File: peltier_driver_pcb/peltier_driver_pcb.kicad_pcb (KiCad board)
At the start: 2 copper layers, 10 parts, among them J1 Conn_01x04, U1 OLED_128x32_I2C, U2 INA260

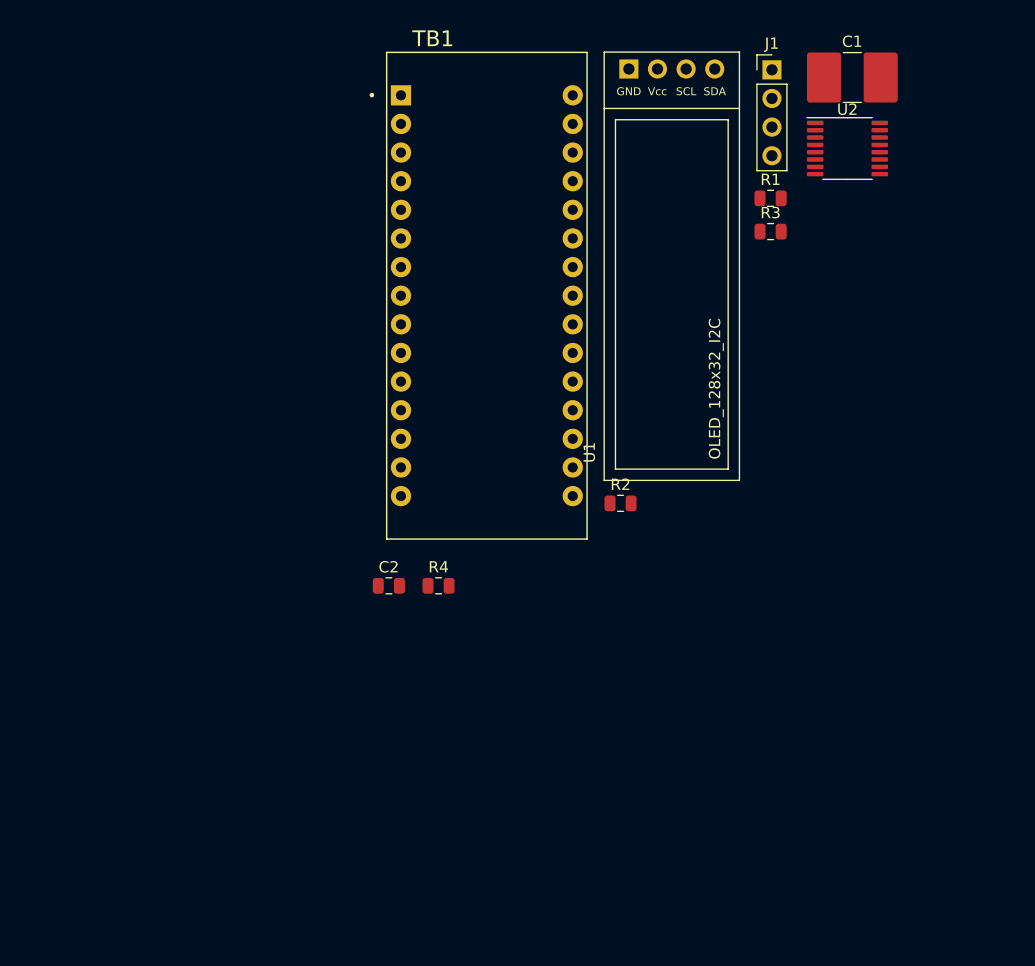
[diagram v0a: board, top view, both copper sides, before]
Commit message: properly saved 3D models to footprint files
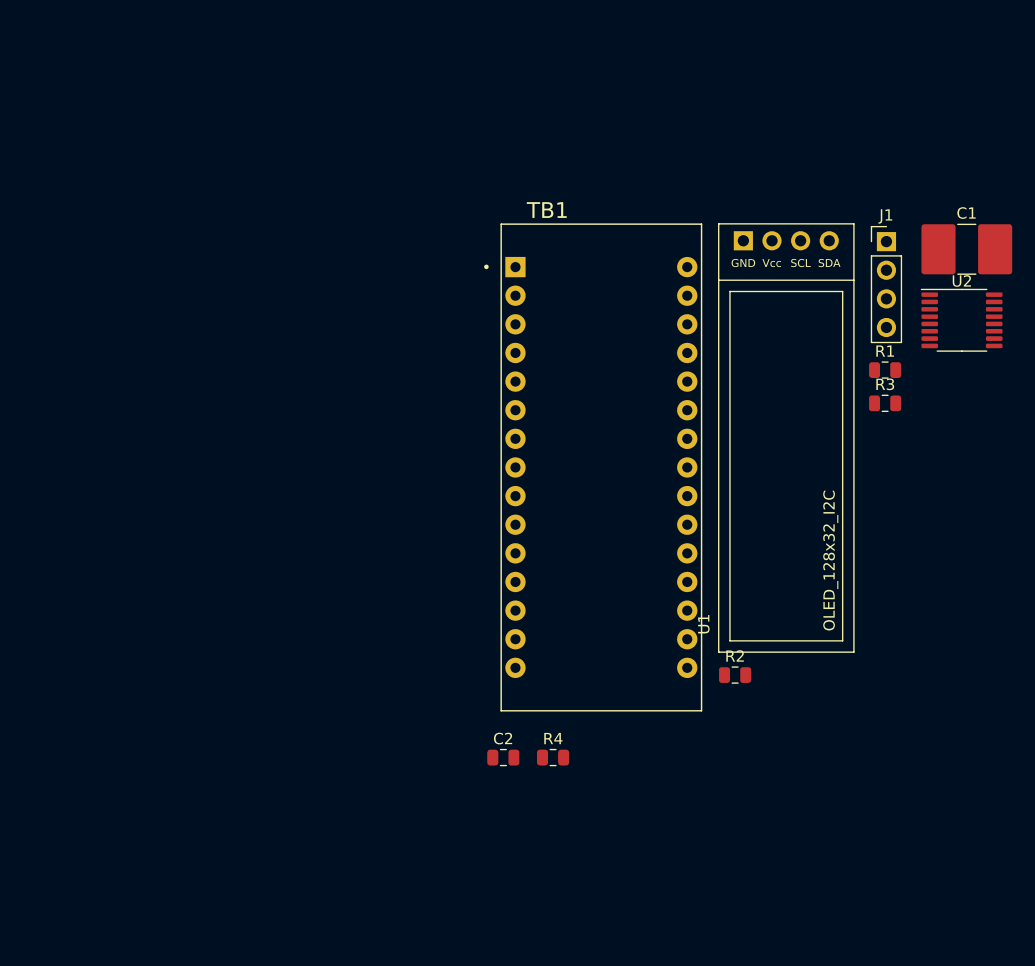
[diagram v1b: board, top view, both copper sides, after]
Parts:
- moved R2 18.3 mm to (167.0, 87.3)
- moved C2 18.3 mm to (146.5, 94.6)
- moved C1 18.3 mm to (187.6, 49.5)
- moved J1 18.3 mm to (180.5, 48.8)
- moved R1 18.3 mm to (180.4, 60.2)
- moved TB1 18.3 mm to (155.2, 68.9)
- moved U1 18.3 mm to (165.6, 47.2)
- moved U2 18.3 mm to (187.2, 55.8)
- moved R3 18.3 mm to (180.4, 63.2)
- moved R4 18.3 mm to (150.9, 94.6)

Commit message: updating PCB
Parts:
- added J2: Temp_sensor_A, Connector_PinHeader_2.54mm:PinHeader_1x02_P2.54mm_Vertical, F.Cu at (113.0, 101.3)
- added J3: Temp_sensor_B, Connector_PinHeader_2.54mm:PinHeader_1x02_P2.54mm_Vertical, F.Cu at (120.1, 101.3)
- added R5: 10k, Resistor_SMD:R_0805_2012Metric, F.Cu at (119.6, 78.7)
- added R6: 10k, Resistor_SMD:R_0805_2012Metric, F.Cu at (121.9, 78.6)
- added R7: 10k, Resistor_SMD:R_0805_2012Metric, F.Cu at (119.6, 82.4)
- added R8: 10k, Resistor_SMD:R_0805_2012Metric, F.Cu at (121.9, 82.4)
- added RV1: 10k, Potentiometer_THT:Potentiometer_Bourns_3296W_Vertical, F.Cu at (114.6, 97.0)
- added RV2: 10k, Potentiometer_THT:Potentiometer_Bourns_3296W_Vertical, F.Cu at (121.5, 97.0)
- moved U2 81.1 mm to (106.6, 65.5), turned to 90 degrees
- moved C1 77.7 mm to (110.0, 53.1)
- moved R3 70.1 mm to (110.4, 67.5), turned to 270 degrees
- moved R1 58.7 mm to (121.9, 54.6), turned to 270 degrees
- moved R2 58.3 mm to (119.4, 53.7), turned to 270 degrees
- moved U1 54.3 mm to (112.0, 56.1)
- moved C2 51.6 mm to (108.3, 59.9), turned to 90 degrees
- moved R4 51.0 mm to (110.4, 63.6), turned to 90 degrees
- moved J1 46.6 mm to (146.1, 80.3), turned to 180 degrees
- moved TB1 23.3 mm to (133.6, 77.7), turned to 180 degrees
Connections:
- C2 pad 1: Net-(C2-Pad1) -> +5V
- R3 pad 1: +5V -> +3V3
- R4 pad 1: +5V -> +3V3
- TB1 pad 23: Net-(TB1-Pad23) -> T_A0
- TB1 pad 24: Net-(TB1-Pad24) -> T_B0
- TB1 pad 25: Net-(TB1-Pad25) -> T_A1
- TB1 pad 26: Net-(TB1-Pad26) -> T_B1
- U2 pad 10: Net-(C2-Pad1) -> +5V
- U2 pad 4: Net-(U2-Pad4) -> GND
- U2 pad 5: Net-(U2-Pad5) -> GND
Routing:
- net SDA: track 0.00 -> 60.1 mm
- net SCL: track 0.00 -> 58.6 mm
- net T_A1: track 0.00 -> 25.7 mm
- net T_B1: track 0.00 -> 19.2 mm
- net T_B0: track 0.00 -> 7.61 mm
- net +3V3: track 0.00 -> 6.50 mm
- net T_A0: track 0.00 -> 6.42 mm
- net +5V: track 0.00 -> 1.86 mm

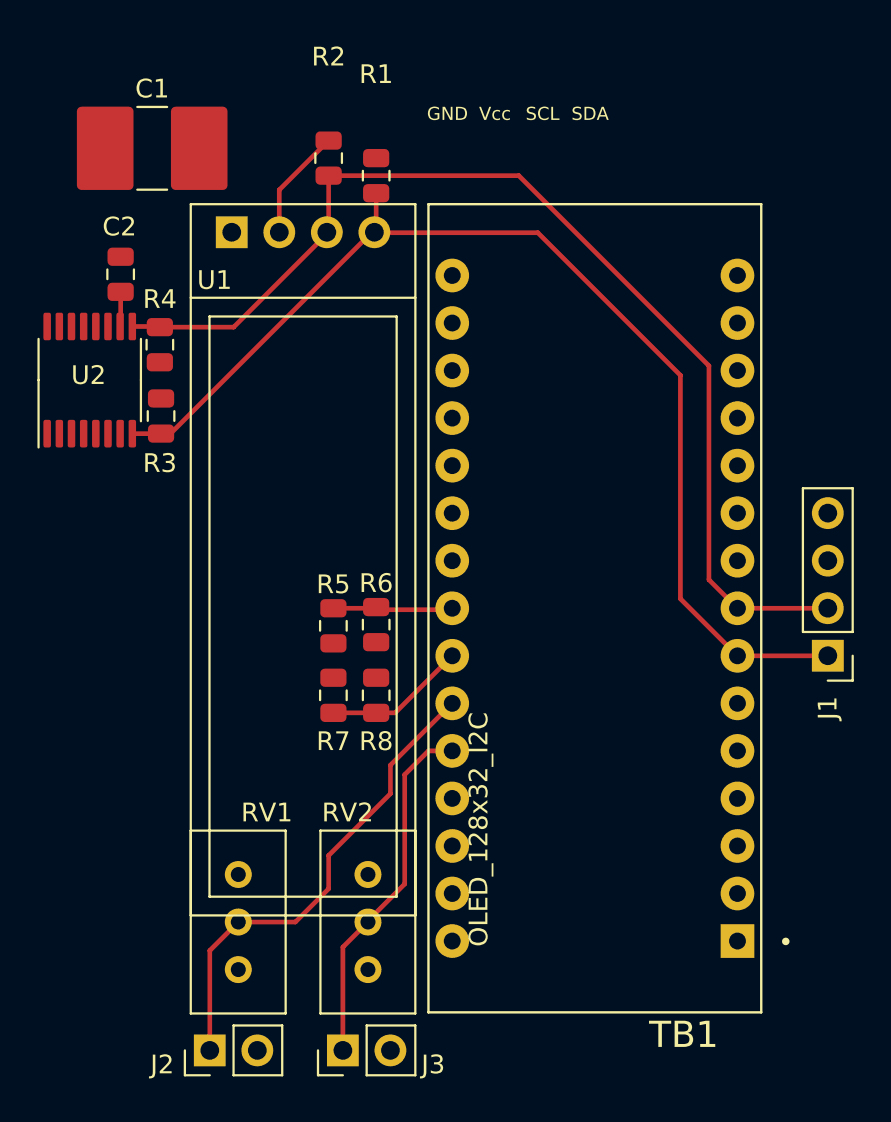
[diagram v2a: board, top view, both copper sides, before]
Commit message: single Pt1000, wheatstone bridge diff amplifier
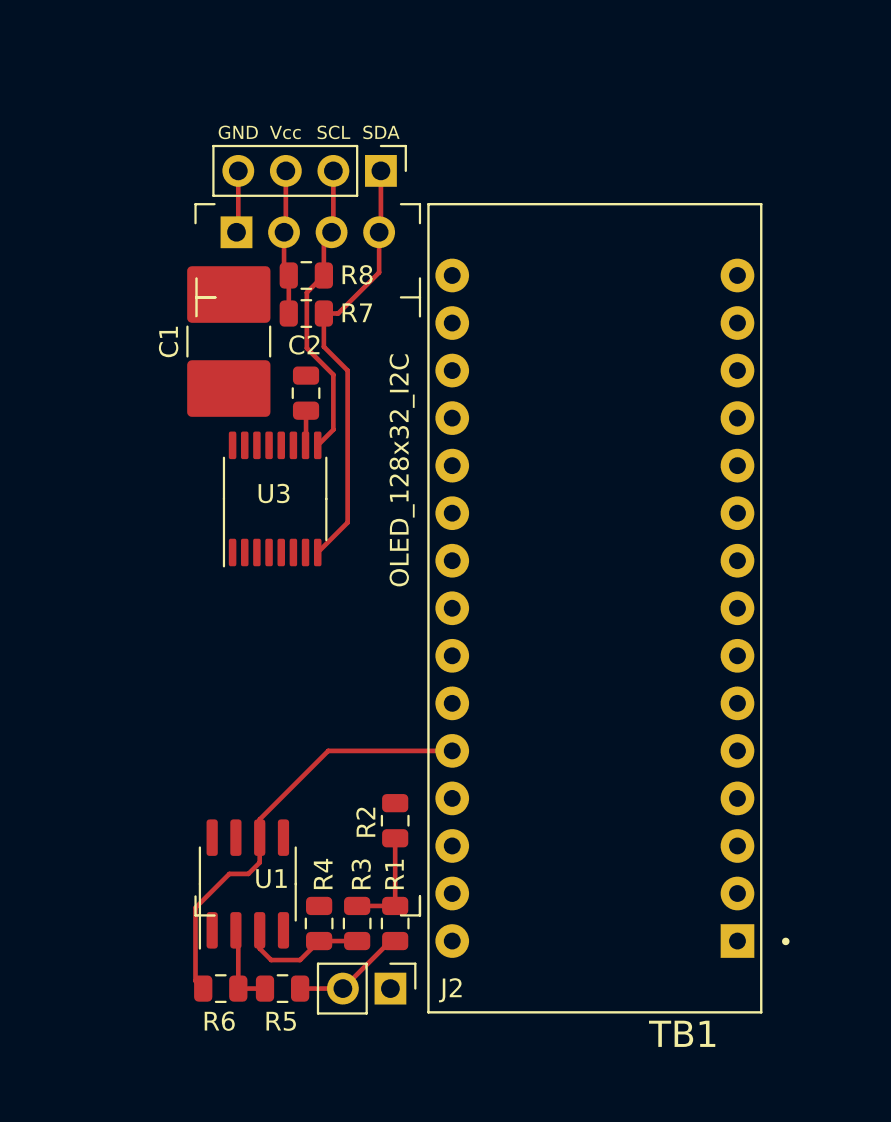
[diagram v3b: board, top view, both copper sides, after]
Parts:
- removed J3: Temp_sensor_B, Connector_PinHeader_2.54mm:PinHeader_1x02_P2.54mm_Vertical
- removed the R7 at (119.6, 82.4)
- removed RV1, RV2: 10k, Potentiometer_THT:Potentiometer_Bourns_3296W_Vertical
- added R3: 1K, Resistor_SMD:R_0805_2012Metric, F.Cu at (120.9, 94.6)
- added U2: OLED_128x32_I2C, peltier_driver_pcb:OLED_128x32_I2C, F.Cu at (112.3, 56.1)
- J2: value Temp_sensor_A -> Pt1000_top
- R1: value 4k7 -> 1K
- R2: value 4k7 -> 4K
- R4: value 4K7 -> 1K
- R5, R6: value 10k -> 100k
- R8: value 10k -> 4K7
- U1: value OLED_128x32_I2C -> MCP601-xSN; footprint peltier_driver_pcb:OLED_128x32_I2C -> Package_SO:SOIC-8_3.9x4.9mm_P1.27mm
- moved R1 40.0 mm to (122.9, 94.6)
- moved U1 36.4 mm to (115.1, 92.5), turned to 90 degrees
- moved R2 35.6 mm to (122.9, 89.1)
- moved J1 35.2 mm to (122.2, 54.4), turned to 270 degrees
- moved R4 32.1 mm to (118.9, 94.6)
- moved R8 22.7 mm to (118.2, 59.9), turned to 0 degrees
- moved R6 21.1 mm to (113.6, 98.0), turned to 0 degrees
- moved R5 19.6 mm to (116.9, 98.0), turned to 0 degrees
- moved C2 11.8 mm to (118.2, 66.2)
- moved U3 11.8 mm to (116.5, 71.9)
- moved C1 11.1 mm to (114.0, 63.5), turned to 90 degrees
- moved J2 10.2 mm to (122.7, 98.0), turned to 270 degrees
- moved R7 9.50 mm to (118.2, 62.0), turned to 0 degrees
- renumbered R3 to R7, U2 to U3
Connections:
- J2 pad 1: T_A1 -> GND
- J2 pad 2: GND -> Net-(J2-Pad2)
- R1 pad 1: +3V3 -> Net-(R1-Pad1)
- R1 pad 2: SDA -> Net-(J2-Pad2)
- R2 pad 1: +3V3 -> +5V
- R2 pad 2: SCL -> Net-(R1-Pad1)
- R4 pad 1: +3V3 -> Net-(R3-Pad2)
- R4 pad 2: SCL -> GND
- R5 pad 1: +5V -> Net-(R5-Pad1)
- R5 pad 2: T_A0 -> Net-(J2-Pad2)
- R6 pad 1: T_A0 -> T_sense
- R6 pad 2: GND -> Net-(R5-Pad1)
- R8 pad 1: T_B0 -> +3V3
- R8 pad 2: GND -> SCL
- TB1 pad 23: T_A0 -> Net-(TB1-Pad23)
- TB1 pad 24: T_B0 -> Net-(TB1-Pad24)
- TB1 pad 25: T_A1 -> Net-(TB1-Pad25)
- TB1 pad 26: T_B1 -> T_sense
- U1 pad 1: +3V3 -> Net-(U1-Pad1)
- U1 pad 2: SCL -> Net-(R5-Pad1)
- U1 pad 3: SDA -> Net-(R3-Pad2)
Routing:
- net SCL: track 58.6 -> 16.2 mm
- net SDA: track 60.1 -> 23.3 mm
- net T_A1: track 25.7 -> 0.00 mm
- net T_sense: track 0.00 -> 23.0 mm
- net T_B1: track 19.2 -> 0.00 mm
- net T_B0: track 7.61 -> 0.00 mm
- net Net-(R3-Pad2): track 0.00 -> 6.86 mm
- net T_A0: track 6.42 -> 0.00 mm
- net Net-(J2-Pad2): track 0.00 -> 6.13 mm
- net Net-(R1-Pad1): track 0.00 -> 5.65 mm
- net Net-(R5-Pad1): track 0.00 -> 4.59 mm
- net GND: track 0.00 -> 3.32 mm
- net +3V3: track 6.50 -> 8.27 mm

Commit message: some tweaks
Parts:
- added V+: Peltier_A, Connector_Pin:Pin_D1.0mm_L10.0mm, F.Cu at (113.0, 77.7)
- added V-: Peltier_B, Connector_Pin:Pin_D1.0mm_L10.0mm, F.Cu at (113.0, 67.1)
- C1: footprint Capacitor_SMD:C_2816_7142Metric -> Capacitor_SMD:C_0805_2012Metric
- moved C1 3.97 mm to (116.1, 66.9)
- moved U3 1.08 mm to (115.6, 72.4)
- moved C2 0.51 mm to (118.1, 66.7)
- moved U1 0.25 mm to (114.8, 92.5)
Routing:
- net SCL: track 16.2 -> 55.0 mm
- net SDA: track 23.3 -> 45.1 mm
- net IN-: track 0.00 -> 2.87 mm
- net IN+: track 0.00 -> 2.87 mm
- net +5V: track 1.86 -> 3.15 mm
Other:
- board outline added: 32.3 x 48.8 mm
- net class Vcc added: clearance 0.2, trace_width 0.5, via_dia 0.8, via_drill 0.4

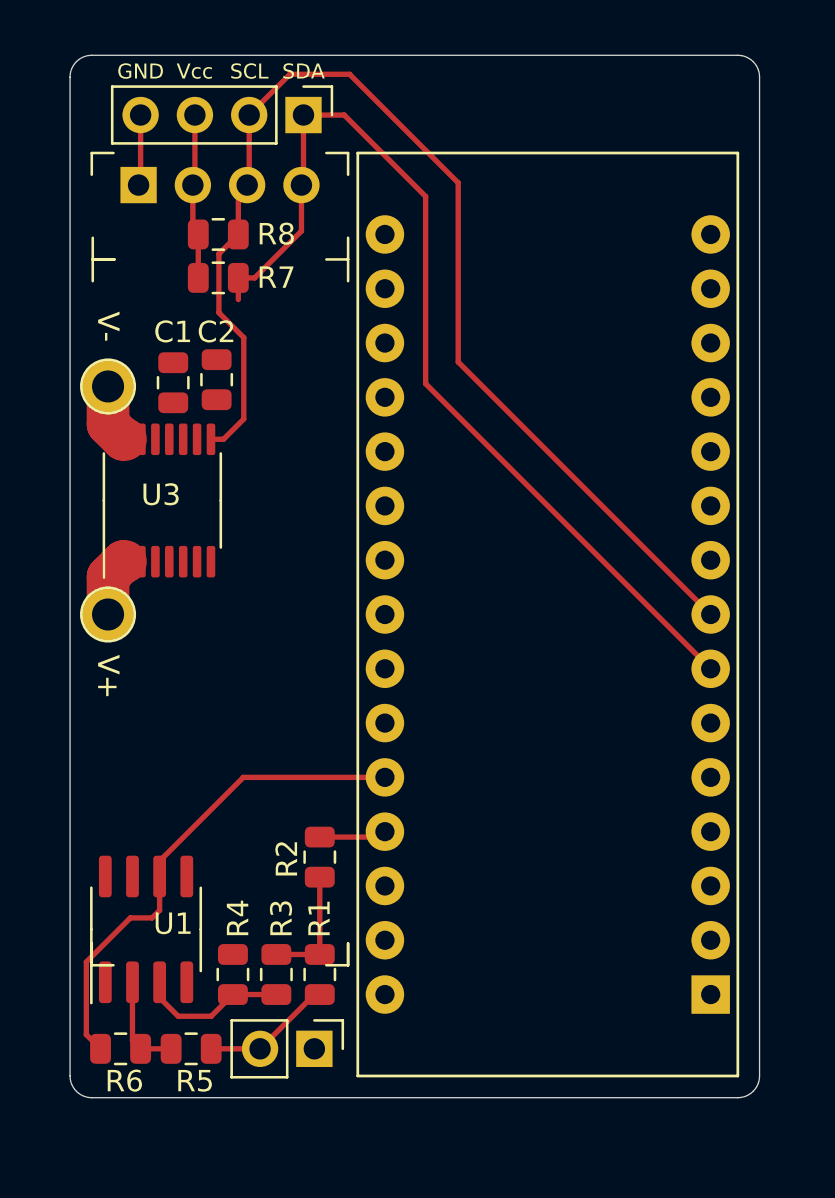
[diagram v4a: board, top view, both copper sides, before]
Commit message: I-source for Pt1000, fixed I2C level mismatch, added mounting holes
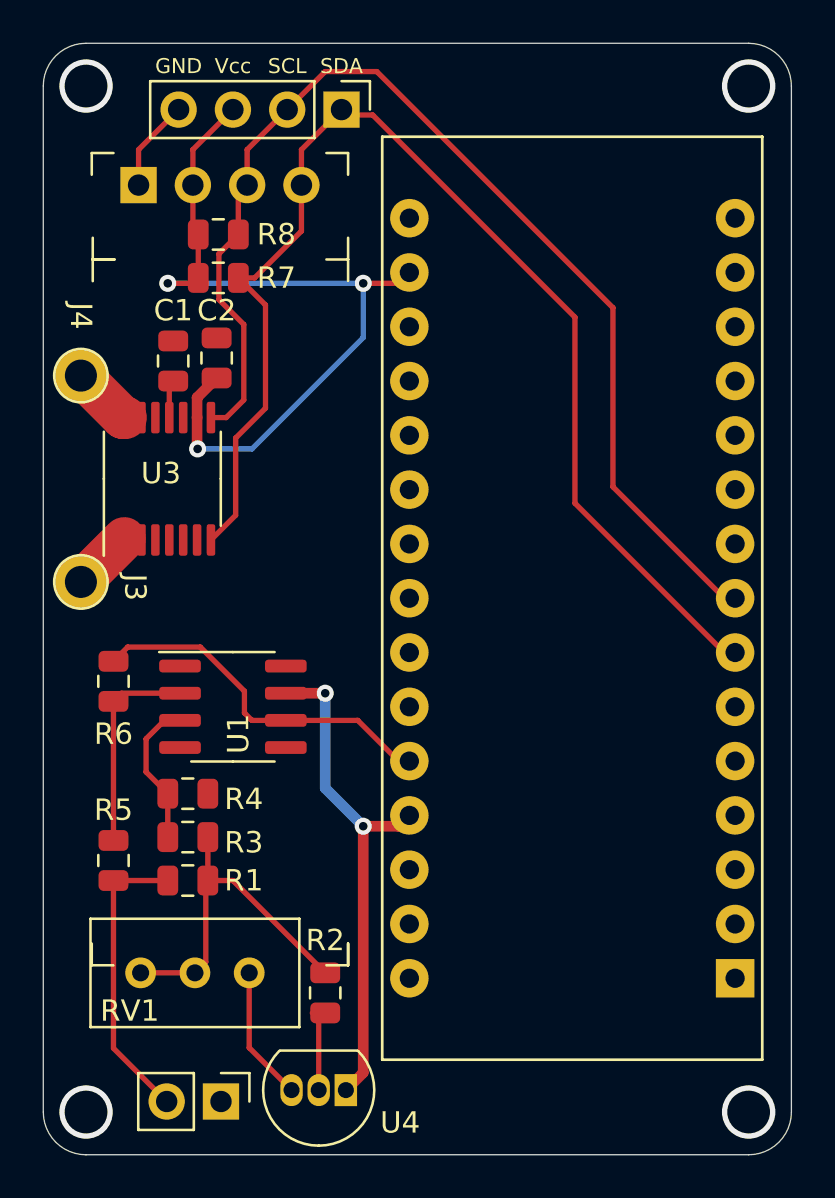
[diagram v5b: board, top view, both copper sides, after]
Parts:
- removed V-: Peltier_B, Connector_Pin:Pin_D1.0mm_L10.0mm
- added J4: Peltier_B, Connector_Pin:Pin_D1.0mm_L10.0mm, F.Cu at (111.8, 66.5)
- added RV1: 3K, Potentiometer_THT:Potentiometer_Bourns_3296W_Vertical, F.Cu at (119.6, 94.5)
- added U4: LM334Z, Package_TO_SOT_THT:TO-92_Inline, F.Cu at (124.2, 100.0)
- R2: value 4K -> 1K
- moved R6 17.2 mm to (113.3, 80.9), turned to 270 degrees
- moved U1 11.2 mm to (118.9, 82.0), turned to 0 degrees
- moved R5 9.53 mm to (113.3, 89.2), turned to 270 degrees
- moved R4 8.72 mm to (116.8, 86.1), turned to 0 degrees
- moved R3 7.65 mm to (116.8, 88.1), turned to 180 degrees
- moved R1 7.58 mm to (116.8, 90.2), turned to 180 degrees
- moved R2 6.36 mm to (123.2, 95.4)
- moved J2 5.02 mm to (118.3, 100.5)
- moved J3 1.98 mm to (111.8, 76.2)
- moved J1 1.80 mm to (124.0, 54.1)
- moved TB1 1.37 mm to (134.7, 77.0)
- moved C2 1.02 mm to (118.1, 65.7)
- moved U3 1.02 mm to (115.6, 71.4)
- moved C1 1.02 mm to (116.1, 65.9)
- renumbered V+ to J3
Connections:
- C2 pad 1: +5V -> +3V3
- R1 pad 1: Net-(R1-Pad1) -> I_ref
- R2 pad 1: +5V -> I_ref
- R2 pad 2: Net-(R1-Pad1) -> Net-(R2-Pad2)
- R3 pad 1: Net-(R1-Pad1) -> I_ref
- U3 pad 10: +5V -> +3V3
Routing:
- net +3V3: track 8.27 -> 38.0 mm, vias 0 -> 3
- net +5V: track 3.15 -> 23.9 mm, vias 0 -> 2
- net I_ref: track 0.00 -> 16.4 mm
- net SDA: track 45.1 -> 58.4 mm
- net Net-(J2-Pad2): track 6.13 -> 14.5 mm
- net Net-(RV1-Pad1): track 0.00 -> 6.31 mm
- net Net-(R1-Pad1): track 5.65 -> 0.00 mm
- net T_sense: track 23.2 -> 17.9 mm
- net Net-(R5-Pad1): track 4.70 -> 9.78 mm
- net Net-(R2-Pad2): track 0.00 -> 4.34 mm
- net Net-(C1-Pad1): track 0.00 -> 1.79 mm
- net GND: track 3.32 -> 4.44 mm
- net SCL: track 55.0 -> 54.4 mm
- net (no net): vias 0 -> 4
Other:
- board size 32.3 x 48.8 mm -> 35 x 52 mm
